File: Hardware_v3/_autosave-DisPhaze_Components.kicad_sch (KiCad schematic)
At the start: 89 parts, among them J1 SWD_Header, J2 USB_B_Micro, J3 PItch_In, J4 PD1_Amt_In, J5 PD2_Amt_In, J6 VCA_In, J7 DAC1_Out, J8 DAC2_Out, J9 Eurorack_16_pin_power, Q1 MMBT3904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

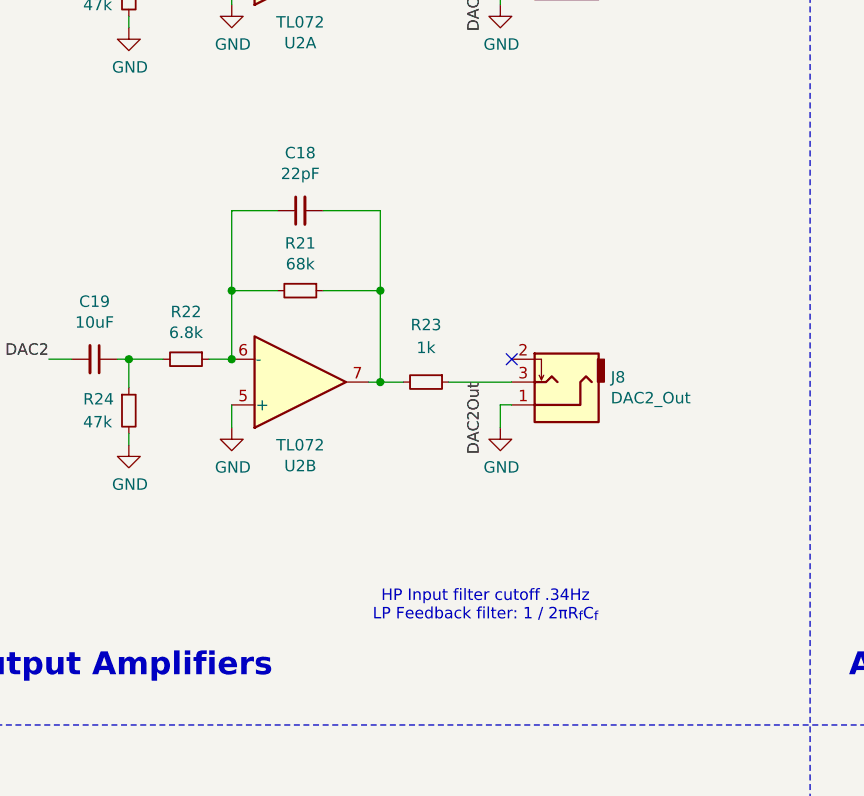
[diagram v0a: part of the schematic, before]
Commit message: Updates to schematic; fixes for stuck MIDI notes
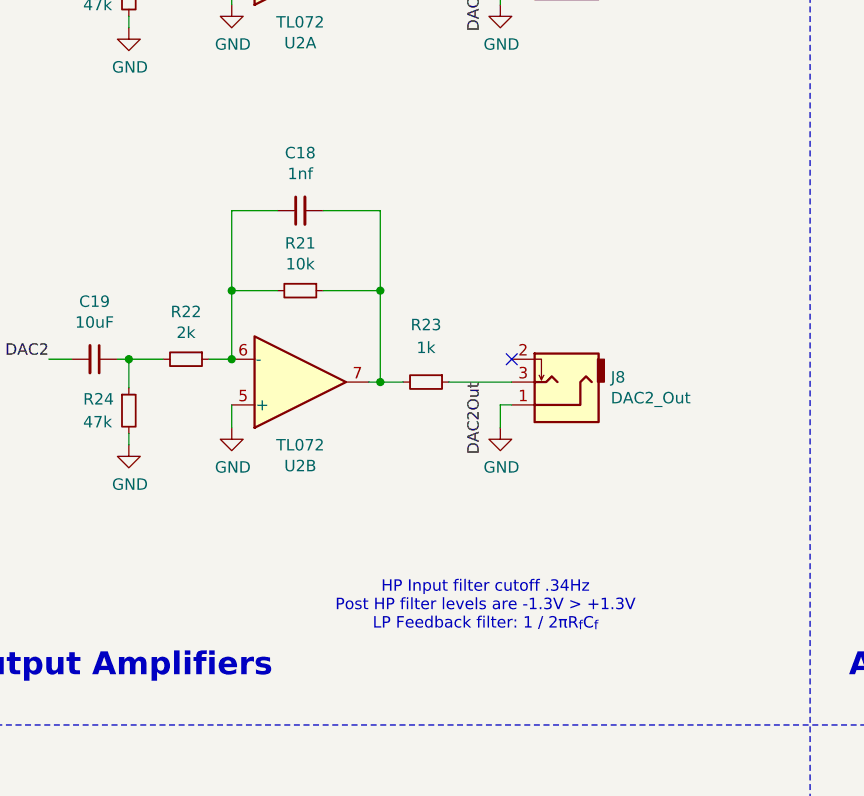
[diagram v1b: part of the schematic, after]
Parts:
- C18: value 22pF -> 1nf
- R21: value 68k -> 10k
- R22: value 6.8k -> 2k
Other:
- note added: "HP Input filter cutoff .34Hz Post HP filter levels are -1.3V > +1.3V LP Feedback filter: 1 / 2πR_{f}C_{f}"
- note removed: "HP Input filter cutoff .34Hz LP Feedback filter: 1 / 2πR_{f}C_{f}"
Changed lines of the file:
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@@
 		)
 	)
-	(text "HP Input filter cutoff .34Hz\nLP Feedback filter: 1 / 2πR_{f}C_{f}"
+	(text "HP Input filter cutoff .34Hz\nPost HP filter levels are -1.3V > +1.3V\nLP Feedback filter: 1 / 2πR_{f}C_{f}"
 		(exclude_from_sim no)
 		(at 265.684 117.602 0)
@@
 			)
 		)
-		(property "Value" "68k"
+		(property "Value" "10k"
 			(at 245.11 79.6036 90)
 			(effects
@@
 			)
 		)
-		(property "Value" "6.8k"
+		(property "Value" "2k"
 			(at 232.41 87.2236 90)
 			(effects
@@
 			)
 		)
-		(property "Value" "22pF"
+		(property "Value" "1nf"
 			(at 245.11 69.5706 90)
 			(effects
